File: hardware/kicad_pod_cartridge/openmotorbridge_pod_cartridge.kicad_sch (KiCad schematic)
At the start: 35 parts, among them Q1 AO3400A, Q2 AO3400A, Q3 AO3400A, Q4 AO3400A, U1 ESP32-C6-MINI-1U, U3 ES8388_Codec, U4 TS5A3159DBVR

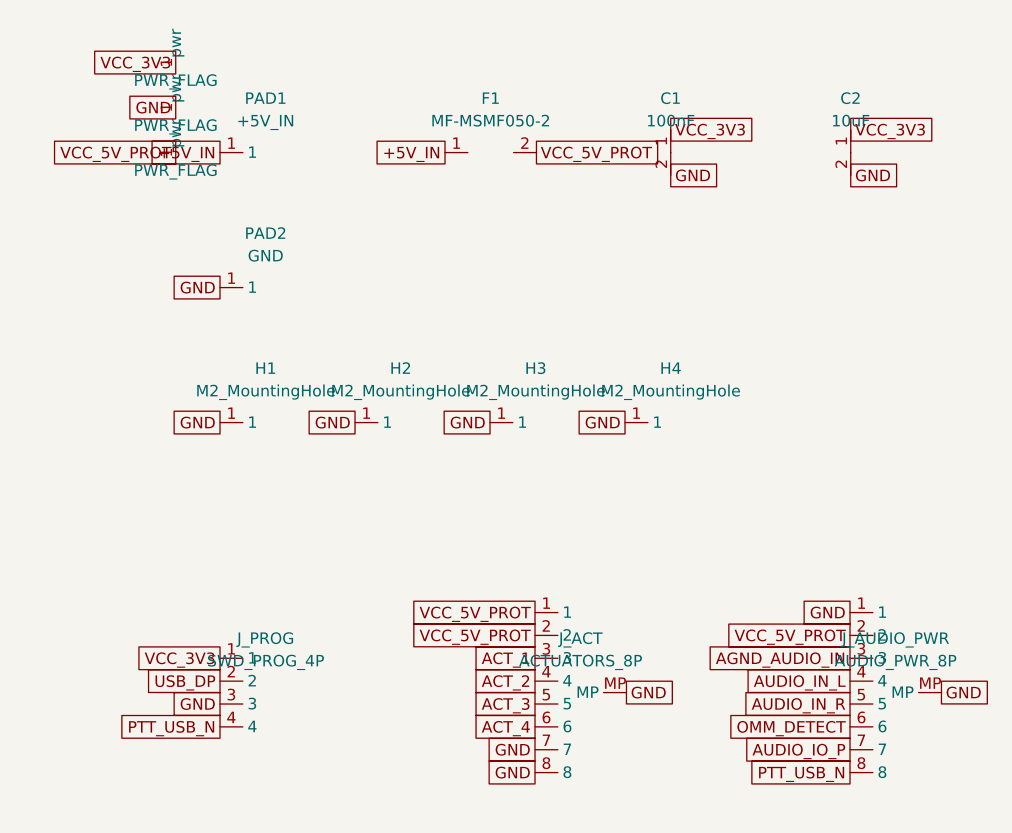
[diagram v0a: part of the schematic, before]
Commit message: feat(cartridge): integrate low-profile automotive dc blade socket J_DC_IN with 3D model, update cad and pcba renders
- Replaced placeholder spring contact pads with low-profile (2.1mm) dual-beam automotive blade slot socket J_DC_IN on PCBA 03 B.Cu, mating with IP67 bulkhead plug CON_POD_DC
- Added realistic 3D VRML model blade_slot_socket_2p.wrl guaranteeing +0.4mm clearance beneath cartridge sled M2 standoffs (h = 2.5mm)
- Aligned OpenSCAD bulkhead partition (002_pod_bulkhead_partition.scad) contact centerline to Z=7.45mm and guide shroud to 2.0mm to eliminate collisions
- Resolved all KiCad prefab-gate plugin blockers (net parity, polyfuse ampacity, J_AUDIO_PWR ground referencing)
- Re-rendered all 3D/orthogonal PCBAs via kicad-cli and updated docs/images/pcba/ and hardware/kicad_*/
- Recompiled production STLs and 3D CAD renders via OpenSCAD and updated docs/images/cad/
- Synchronized BOM database, JLCPCB production packages, and bilingual documentation (DE/EN)
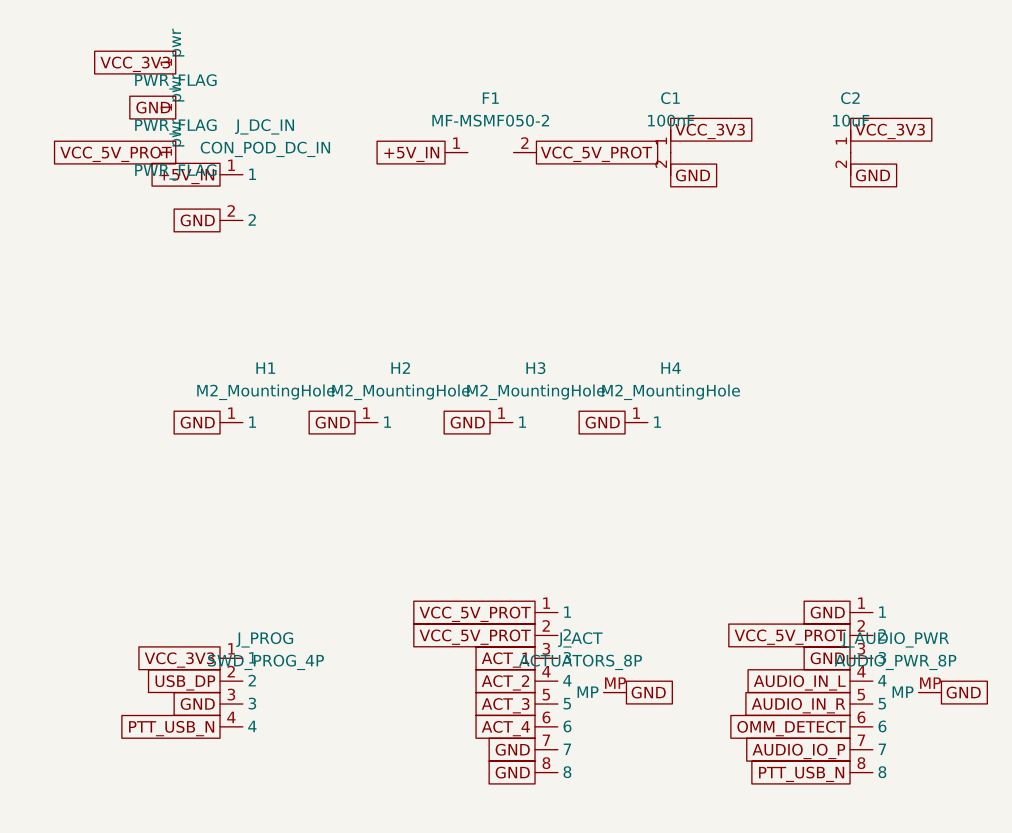
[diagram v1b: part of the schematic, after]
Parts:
- removed PAD2: GND, TestPoint:TestPoint_Pad_D3.0mm_OD3.5mm, symbol Connector:Conn_01x01
- F1: Spec (none) -> IT 1.0 A
- J_DC_IN: renamed from PAD1; value +5V_IN -> CON_POD_DC_IN; footprint TestPoint:TestPoint_Pad_D3.0mm_OD3.5mm -> Connector:Blade_Slot_Socket_1x02_P10.0mm_Horizontal_SMD; symbol Connector:Conn_01x01 -> Connector:Blade_Slot_Socket_1x02
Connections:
- net AGND_AUDIO_IN is gone; now on net GND: J_AUDIO_PWR.3
- net GND: now also J_DC_IN.2
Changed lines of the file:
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@@
 		(property "Value" "MF-MSMF050-2" (at 65.00 36.50 0) (effects (font (size 1.27 1.27))))
 		(property "Footprint" "Fuse:Fuse_1812_4532Metric" (at 65.00 40.00 0) (effects (font (size 1.27 1.27)) hide))
+		(property "Spec" "IT 1.0 A" (at 65.00 42.00 0) (effects (font (size 1.27 1.27)) hide))
 		(pin "1")
 		(pin "2")
@@
 		(pin "4")
 	)
-	(symbol (lib_id "Connector:Conn_01x01") (at 40.00 40.00 0) (unit 1)
-		(in_bom yes) (on_board yes) (dnp no)
-		(property "Reference" "PAD1" (at 40.00 34.00 0) (effects (font (size 1.27 1.27))))
-		(property "Value" "+5V_IN" (at 40.00 36.50 0) (effects (font (size 1.27 1.27))))
-		(property "Footprint" "TestPoint:TestPoint_Pad_D3.0mm_OD3.5mm" (at 40.00 40.00 0) (effects (font (size 1.27 1.27)) hide))
-		(pin "1")
-	)
-	(symbol (lib_id "Connector:Conn_01x01") (at 40.00 55.00 0) (unit 1)
-		(in_bom yes) (on_board yes) (dnp no)
-		(property "Reference" "PAD2" (at 40.00 49.00 0) (effects (font (size 1.27 1.27))))
-		(property "Value" "GND" (at 40.00 51.50 0) (effects (font (size 1.27 1.27))))
-		(property "Footprint" "TestPoint:TestPoint_Pad_D3.0mm_OD3.5mm" (at 40.00 55.00 0) (effects (font (size 1.27 1.27)) hide))
-		(pin "1")
+	(symbol (lib_id "Connector:Blade_Slot_Socket_1x02") (at 40.00 45.00 0) (unit 1)
+		(in_bom yes) (on_board yes) (dnp no)
+		(property "Reference" "J_DC_IN" (at 40.00 37.00 0) (effects (font (size 1.27 1.27))))
+		(property "Value" "CON_POD_DC_IN" (at 40.00 39.50 0) (effects (font (size 1.27 1.27))))
+		(property "Footprint" "Connector:Blade_Slot_Socket_1x02_P10.0mm_Horizontal_SMD" (at 40.00 45.00 0) (effects (font (size 1.27 1.27)) hide))
+		(property "Datasheet" "https://openmotorbridge.org/hw/cots_pod_dc_blade_plug" (at 40.00 45.00 0) (effects (font (size 1.27 1.27)) hide))
+		(property "Description" "2-Pin Automotive Dual-Beam Blade Slot Socket (10.0mm Pitch, 5A, Mates with CON_POD_DC)" (at 40.00 45.00 0) (effects (font (size 1.27 1.27)) hide))
+		(pin "1")
+		(pin "2")
 	)
 	(symbol (lib_id "Transistor_FET:AO3400A") (at 40.00 160.00 0) (unit 1)
@@
 	(global_label "GND" (shape passive) (at 104.92 91.11 180) (effects (font (size 1.27 1.27)) (justify right)))
 	(global_label "VCC_5V_PROT" (shape passive) (at 104.92 93.65 180) (effects (font (size 1.27 1.27)) (justify right)))
-	(global_label "AGND_AUDIO_IN" (shape passive) (at 104.92 96.19 180) (effects (font (size 1.27 1.27)) (justify right)))
+	(global_label "GND" (shape passive) (at 104.92 96.19 180) (effects (font (size 1.27 1.27)) (justify right)))
 	(global_label "AUDIO_IN_L" (shape passive) (at 104.92 98.73 180) (effects (font (size 1.27 1.27)) (justify right)))
 	(global_label "AUDIO_IN_R" (shape passive) (at 104.92 101.27 180) (effects (font (size 1.27 1.27)) (justify right)))
@@
 	(global_label "GND" (shape passive) (at 34.92 101.27 180) (effects (font (size 1.27 1.27)) (justify right)))
 	(global_label "PTT_USB_N" (shape passive) (at 34.92 103.81 180) (effects (font (size 1.27 1.27)) (justify right)))
-	(global_label "+5V_IN" (shape passive) (at 34.92 40.00 180) (effects (font (size 1.27 1.27)) (justify right)))
-	(global_label "GND" (shape passive) (at 34.92 55.00 180) (effects (font (size 1.27 1.27)) (justify right)))
+	(global_label "+5V_IN" (shape passive) (at 34.92 42.46 180) (effects (font (size 1.27 1.27)) (justify right)))
+	(global_label "GND" (shape passive) (at 34.92 47.54 180) (effects (font (size 1.27 1.27)) (justify right)))
 	(global_label "Q1_GATE" (shape passive) (at 34.92 160.00 180) (effects (font (size 1.27 1.27)) (justify right)))
 	(global_label "GND" (shape passive) (at 42.54 165.08 0) (effects (font (size 1.27 1.27)) (justify left)))

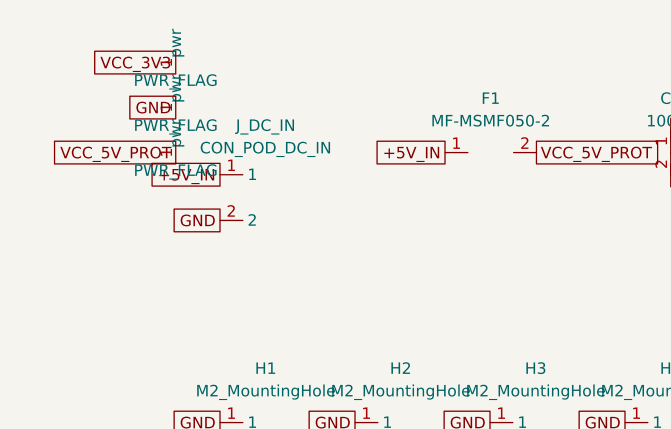
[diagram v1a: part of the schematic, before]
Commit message: feat(cartridge): switch J_AUDIO_PWR and J_ACT to vertical BM08B-SRSS top-entry headers
- replace horizontal SM08B headers on PCBA 03 with vertical BM08B-SRSS-TB (C160404)
- preserve exact signal pad micrometer coordinates (X=105.375 and X=130.000)
- keep cartridge sled length strictly unchanged at 75.0 mm
- update 3D step models, PCB routing clearances, zones and schematic parity
- update CAD dummy PCB with vertical top-entry bodies and gold contacts
- regenerate JLCPCB manufacturing packages (BOM, CPL, Gerber packages)
- update data/bom_parts.json, webapp_pwa/js/bom_catalog.js and docs (15_bom, 07_pinouts)
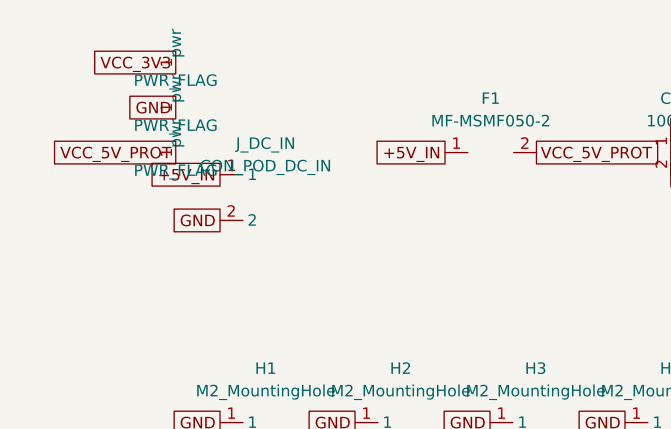
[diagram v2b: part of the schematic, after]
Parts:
- removed J_ACT: ACTUATORS_8P, Connector_JST:JST_SH_SM08B-SRSS-TB_1x08-1MP_P1.00mm_Horizontal, symbol Connector_JST:JST_SH_SM08B_Shielded
- removed J_AUDIO_PWR: AUDIO_PWR_8P, Connector_JST:JST_SH_SM08B-SRSS-TB_1x08-1MP_P1.00mm_Horizontal, symbol Connector_JST:JST_SH_SM08B_Shielded
- added J_ACT: ACTUATORS_8P, Connector_JST:JST_SH_BM08B-SRSS-TB_1x08-1MP_P1.00mm_Vertical, symbol Connector_JST:JST_SH_BM08B_Shielded
- added J_AUDIO_PWR: AUDIO_PWR_8P, Connector_JST:JST_SH_BM08B-SRSS-TB_1x08-1MP_P1.00mm_Vertical, symbol Connector_JST:JST_SH_BM08B_Shielded
- F1: Spec IT 1.0 A -> (none)
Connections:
- net ACT_1: now also J_ACT.3
- net ACT_2: now also J_ACT.4
- net ACT_3: now also J_ACT.5
- net ACT_4: now also J_ACT.6
- net AUDIO_IN_L: now also J_AUDIO_PWR.4
- net AUDIO_IN_R: now also J_AUDIO_PWR.5
- net AUDIO_IO_P: now also J_AUDIO_PWR.7
- net GND: now also J_ACT.7, J_ACT.8, J_ACT.MP, J_AUDIO_PWR.1, J_AUDIO_PWR.3, J_AUDIO_PWR.MP
- net OMM_DETECT: now also J_AUDIO_PWR.6
- net PTT_USB_N: now also J_AUDIO_PWR.8
- net VCC_5V_PROT: now also J_ACT.1, J_ACT.2, J_AUDIO_PWR.2

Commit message: feat(pcba03,pod): align hardware pinouts, center vertical port stack, and sync 3D CAD/PCBA renders
- Reconcile PCBA 03 pinouts (J_BUS, J_USB_OUT, J_ACT 8-pin 4-channel, J_AUDIO_PWR) with German and English documentation
- Center Port A (Bus, upper Z=26.5mm) and Port B (USB-C, lower Z=11.5mm) horizontally at Y=35.0mm on short bulkhead wall
- Update OpenSCAD models (pod_base_housing.scad, 001_pod_rear_m8_gland.scad, assemblies, dummy_adapter_pcb.scad)
- Recompile all 90 production STLs and 51 3D CAD renders
- Raytrace and sync all 3D PCBA views across docs/images/pcba/
- Pass prefab-gate verification with 0 blocking findings
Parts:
- removed ANT_UWB: Taoglas_FXUWB10, Connector_Coaxial:U.FL_Hirose_U.FL-R-SMT-1_Vertical, symbol Connector_Coaxial:U.FL
- removed C1: 100nF, Capacitor_SMD:C_0603_1608Metric, symbol Device:C_Small
- removed C2: 10uF, Capacitor_SMD:C_0805_2012Metric, symbol Device:C_Small
- removed D1, D2, D3, D4: 1N4148WS, Diode_SMD:D_SOD-323, symbol Diode:1N4148WS
- removed F1: MF-MSMF050-2, Fuse:Fuse_1812_4532Metric, symbol Device:Polyfuse_Small
- removed H1, H2, H3, H4: M2_MountingHole, MountingHole:MountingHole_2.2mm_M2_Pad, symbol Mechanical:MountingHole_Pad
- removed J_ACT: ACTUATORS_8P, Connector_JST:JST_SH_BM08B-SRSS-TB_1x08-1MP_P1.00mm_Vertical, symbol Connector_JST:JST_SH_BM08B_Shielded
- removed J_AUDIO_PWR: AUDIO_PWR_8P, Connector_JST:JST_SH_BM08B-SRSS-TB_1x08-1MP_P1.00mm_Vertical, symbol Connector_JST:JST_SH_BM08B_Shielded
- removed J_DC_IN: CON_POD_DC_IN, Connector:Blade_Slot_Socket_1x02_P10.0mm_Horizontal_SMD, symbol Connector:Blade_Slot_Socket_1x02
- removed J_PROG: SWD_PROG_4P, Connector_PinHeader_1.27mm:PinHeader_1x04_P1.27mm_Vertical_SMD_Pin1Left, symbol Connector_PinHeader:PinHeader_1x04
- removed Q1, Q2, Q3, Q4: AO3400A, Package_TO_SOT_SMD:SOT-23, symbol Transistor_FET:AO3400A
- removed R1, R2, R3, R4: 100R, Resistor_SMD:R_0603_1608Metric, symbol Device:R_Small
- removed R5, R6, R7, R8: 100k, Resistor_SMD:R_0603_1608Metric, symbol Device:R_Small
- removed R9: 10k, Resistor_SMD:R_0603_1608Metric, symbol Device:R_Small
- removed U1: ESP32-C6-MINI-1U, RF_Module:ESP32-S2-MINI-1U, symbol MCU:ESP32-C6-MINI-1U
- removed U3: ES8388_Codec, Package_DFN_QFN:QFN-28-1EP_4x4mm_P0.4mm_EP2.4x2.4mm, symbol Audio:ES8388_Codec
- removed U4: TS5A3159DBVR, Package_TO_SOT_SMD:SOT-23-6, symbol Switch:TS5A3159_SPDT
- removed U_UWB: DW3110, Package_DFN_QFN:QFN-16-1EP_3x3mm_P0.5mm_EP1.7x1.7mm_ThermalVias, symbol RF_Module:DW3110
- removed Y_UWB: 38.4MHz, Crystal:Crystal_SMD_2016-4Pin_2.0x1.6mm, symbol Device:Crystal_4Pin
- added C_PD_IN: 22uF_25V, C_1210_3225Metric, symbol C_PD_IN_sym
- added C_PD_OUT: 47uF_25V, C_1210_3225Metric, symbol C_PD_OUT_sym
- added D1: 1N4148WS, D_SOD-323, symbol D1_sym
- added D2: 1N4148WS, D_SOD-323, symbol D2_sym
- added D3: 1N4148WS, D_SOD-323, symbol D3_sym
- added D4: 1N4148WS, D_SOD-323, symbol D4_sym
- added F1: MF-MSMF050-2, Fuse_1812_4532Metric, symbol F1_sym
- added H1: M2.5_MountingHole, MountingHole_2.7mm_M2.5_Pad, symbol H1_sym
- added H2: M2.5_MountingHole, MountingHole_2.7mm_M2.5_Pad, symbol H2_sym
- added H3: M2.5_MountingHole, MountingHole_2.7mm_M2.5_Pad, symbol H3_sym
- added H4: M2.5_MountingHole, MountingHole_2.7mm_M2.5_Pad, symbol H4_sym
- added J_ACT: ACTUATORS_8P, JST_SH_BM08B-SRSS-TB_1x08-1MP_P1.00mm_Vertical, symbol J_ACT_sym
- added J_AUDIO_PWR: AUDIO_PWR_8P, JST_SH_BM08B-SRSS-TB_1x08-1MP_P1.00mm_Vertical, symbol J_AUDIO_PWR_sym
- added J_BUS: 4-PIN_BUS_IN, JST_GH_BM04B-GHS-TBT_1x04-1MP_P1.25mm_Vertical, symbol J_BUS_sym
- added J_USB_OUT: 30W_PD_OUT, JST_GH_BM04B-GHS-TBT_1x04-1MP_P1.25mm_Vertical, symbol J_USB_OUT_sym
- added L_PD: 10uH_7x7mm, L_Wuerth_WE-PD-Typ-7345, symbol L_PD_sym
- added Q1: AO3400A, SOT-23, symbol Q1_sym
- added Q2: AO3400A, SOT-23, symbol Q2_sym
- added Q3: AO3400A, SOT-23, symbol Q3_sym
- added Q4: AO3400A, SOT-23, symbol Q4_sym
- added R1: 100R, R_0603_1608Metric, symbol R1_sym
- added R2: 100R, R_0603_1608Metric, symbol R2_sym
- added R3: 100R, R_0603_1608Metric, symbol R3_sym
- added R4: 100R, R_0603_1608Metric, symbol R4_sym
- added R5: 100k, R_0603_1608Metric, symbol R5_sym
- added R6: 100k, R_0603_1608Metric, symbol R6_sym
- added R7: 100k, R_0603_1608Metric, symbol R7_sym
- added R8: 100k, R_0603_1608Metric, symbol R8_sym
- added R9: 100k, R_0603_1608Metric, symbol R9_sym
- added U1: ESP32-Host-MCU, ESP32-C6-MINI-1, symbol U1_sym
- added U3: ES8388_Codec, QFN-28-1EP_4x4mm_P0.4mm_EP2.4x2.4mm, symbol U3_sym
- added U4: TS5A3159_SPDT, SOT-23-6, symbol U4_sym
- added U_PD: SW3516_PD30W, QFN-32-1EP_5x5mm_P0.5mm_EP3.45x3.45mm_ThermalVias, symbol U_PD_sym
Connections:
- net ACT1_GATE: now also R1.1 (ACT1_GATE), U1.18 (ACT1_GATE)
- net ACT2_GATE: now also R2.1 (ACT2_GATE), U1.19 (ACT2_GATE)
- net ACT3_GATE: now also R3.1 (ACT3_GATE), U1.8 (ACT3_GATE)
- net ACT4_GATE: now also R4.1 (ACT4_GATE), U1.9 (ACT4_GATE)
- net ACT_1: now also D1.1 (ACT_1), J_ACT.6 (ACT_1), Q1.3 (ACT_1)
- net ACT_2: now also D2.1 (ACT_2), J_ACT.5 (ACT_2), Q2.3 (ACT_2)
- net ACT_3: now also D3.1 (ACT_3), J_ACT.4 (ACT_3), Q3.3 (ACT_3)
- net ACT_4: now also D4.1 (ACT_4), J_ACT.3 (ACT_4), Q4.3 (ACT_4)
- net AUDIO_IN_L: now also J_AUDIO_PWR.4 (AUDIO_IN_L), U3.8 (AUDIO_IN_L)
- net AUDIO_IN_R: now also J_AUDIO_PWR.5 (AUDIO_IN_R), U3.9 (AUDIO_IN_R)
- net AUDIO_IO_P: now also J_AUDIO_PWR.7 (AUDIO_IO_P), U3.17 (AUDIO_IO_P), U4.2 (AUDIO_IO_P)
- net GND: now also C_PD_IN.2 (GND), C_PD_OUT.2 (GND), H1.1 (GND), H2.1 (GND), H3.1 (GND), H4.1 (GND), J_ACT.1 (GND), J_ACT.2 (GND), J_ACT.MP (GND), J_AUDIO_PWR.1 (GND), J_AUDIO_PWR.3 (GND), J_AUDIO_PWR.MP (GND), J_BUS.2 (GND), J_BUS.MP (GND), J_USB_OUT.2 (GND), J_USB_OUT.MP (GND), Q1.2 (GND), Q2.2 (GND), Q3.2 (GND), Q4.2 (GND), R5.2 (GND), R6.2 (GND), R7.2 (GND), R8.2 (GND), U1.1 (GND), U1.10 (GND), U1.11 (GND), U1.12 (GND), U1.13 (GND), U1.26 (GND), U1.27 (GND), U1.28 (GND), U1.29 (GND), U1.30 (GND), U1.31 (GND), U1.32 (GND), U1.33 (GND), U1.34 (GND), U1.35 (GND), U1.36 (GND), U1.37 (GND), U1.38 (GND), U1.39 (GND), U1.4 (GND), U1.40 (GND), U1.41 (GND), U1.42 (GND), U1.43 (GND), U1.44 (GND), U1.45 (GND), U1.46 (GND), U1.47 (GND), U1.48 (GND), U1.49 (GND), U1.5 (GND), U1.50 (GND), U1.51 (GND), U1.52 (GND), U1.53 (GND), U1.54 (GND), U1.55 (GND), U1.56 (GND), U1.57 (GND), U1.58 (GND), U1.59 (GND), U1.6 (GND), U1.60 (GND), U1.61 (GND), U1.62 (GND), U1.63 (GND), U1.64 (GND), U1.65 (GND), U3.10 (GND), U3.14 (GND), U3.15 (GND), U3.16 (GND), U3.18 (GND), U3.22 (GND), U3.24 (GND), U3.25 (GND), U3.26 (GND), U3.27 (GND), U3.28 (GND), U3.29 (GND), U3.7 (GND), U4.5 (GND), U_PD.10 (GND), U_PD.11 (GND), U_PD.12 (GND), U_PD.19 (GND), U_PD.20 (GND), U_PD.21 (GND), U_PD.22 (GND), U_PD.23 (GND), U_PD.24 (GND), U_PD.25 (GND), U_PD.26 (GND), U_PD.27 (GND), U_PD.28 (GND), U_PD.29 (GND), U_PD.30 (GND), U_PD.31 (GND), U_PD.32 (GND), U_PD.33 (GND), U_PD.5 (GND), U_PD.6 (GND), U_PD.7 (GND), U_PD.8 (GND), U_PD.9 (GND)
- net I2C_SCL: now also U1.17 (I2C_SCL), U3.20 (I2C_SCL)
- net I2C_SDA: now also U1.25 (I2C_SDA), U3.21 (I2C_SDA)
- net I2S_BCLK: now also U1.21 (I2S_BCLK), U3.2 (I2S_BCLK)
- net I2S_DIN: now also U1.24 (I2S_DIN), U3.4 (I2S_DIN)
- net I2S_DOUT: now also U1.23 (I2S_DOUT), U3.5 (I2S_DOUT)
- net I2S_MCLK: now also U1.20 (I2S_MCLK), U3.1 (I2S_MCLK)
- net I2S_WS: now also U1.22 (I2S_WS), U3.3 (I2S_WS)
- net OMM_DETECT: now also J_AUDIO_PWR.6 (OMM_DETECT), R9.1 (OMM_DETECT), U1.16 (OMM_DETECT), U3.13 (OMM_DETECT), U4.3 (OMM_DETECT)
- net Q1_GATE: now also Q1.1 (Q1_GATE), R1.2 (Q1_GATE), R5.1 (Q1_GATE)
- net Q2_GATE: now also Q2.1 (Q2_GATE), R2.2 (Q2_GATE), R6.1 (Q2_GATE)
- net Q3_GATE: now also Q3.1 (Q3_GATE), R3.2 (Q3_GATE), R7.1 (Q3_GATE)
- net Q4_GATE: now also Q4.1 (Q4_GATE), R4.2 (Q4_GATE), R8.1 (Q4_GATE)
- net USB_DP: now also J_BUS.3 (USB_DP), U1.15 (USB_DP), U4.1 (USB_DP)
- net VCC_3V3: now also R9.2 (VCC_3V3), U1.2 (VCC_3V3), U1.3 (VCC_3V3), U3.11 (VCC_3V3), U3.19 (VCC_3V3), U3.23 (VCC_3V3), U3.6 (VCC_3V3), U4.4 (VCC_3V3)
- net VCC_5V_PROT: now also D1.2 (VCC_5V_PROT), D2.2 (VCC_5V_PROT), D3.2 (VCC_5V_PROT), D4.2 (VCC_5V_PROT), F1.2 (VCC_5V_PROT), J_ACT.7 (VCC_5V_PROT), J_ACT.8 (VCC_5V_PROT), J_AUDIO_PWR.2 (VCC_5V_PROT)
- net VOICE_OUT: now also U3.12 (VOICE_OUT), U4.6 (VOICE_OUT)
- new net CC1: J_USB_OUT.3 (CC1), U_PD.15 (CC1)
- new net CC2: J_USB_OUT.4 (CC2), U_PD.16 (CC2)
- new net PTT_BTN: J_AUDIO_PWR.8 (PTT_BTN), U1.7 (PTT_BTN)
- new net SW_NODE: L_PD.1 (SW_NODE), U_PD.3 (SW_NODE), U_PD.4 (SW_NODE)
- new net USB_DM: J_BUS.4 (USB_DM), U1.14 (USB_DM)
- new net VBUS_30W: C_PD_IN.1 (VBUS_30W), C_PD_OUT.1 (VBUS_30W), F1.1 (VBUS_30W), J_USB_OUT.1 (VBUS_30W), L_PD.2 (VBUS_30W), U_PD.13 (VBUS_30W), U_PD.14 (VBUS_30W)
- new net VCC_BUS: J_BUS.1 (VCC_BUS), U_PD.1 (VCC_BUS), U_PD.2 (VCC_BUS)
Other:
- title: OpenMotorBridge PCBA 03 - Universal Smart Modular Cartridge Rev 3.0 -> OpenMotorBridge Satellite Pod Interface (PCBA 03)
